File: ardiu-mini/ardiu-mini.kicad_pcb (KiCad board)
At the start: 2 copper layers, 69.9 x 25.4 mm, 39 parts, among them J1 Micro_SD_Card_Det, J2 ICSP, J3 Conn_01x06_Female, Q1 AO4838, Q2 AO4838, SW1 SW_Push, U1 ATmega328PB-A, U2 AP7375-33SA-7

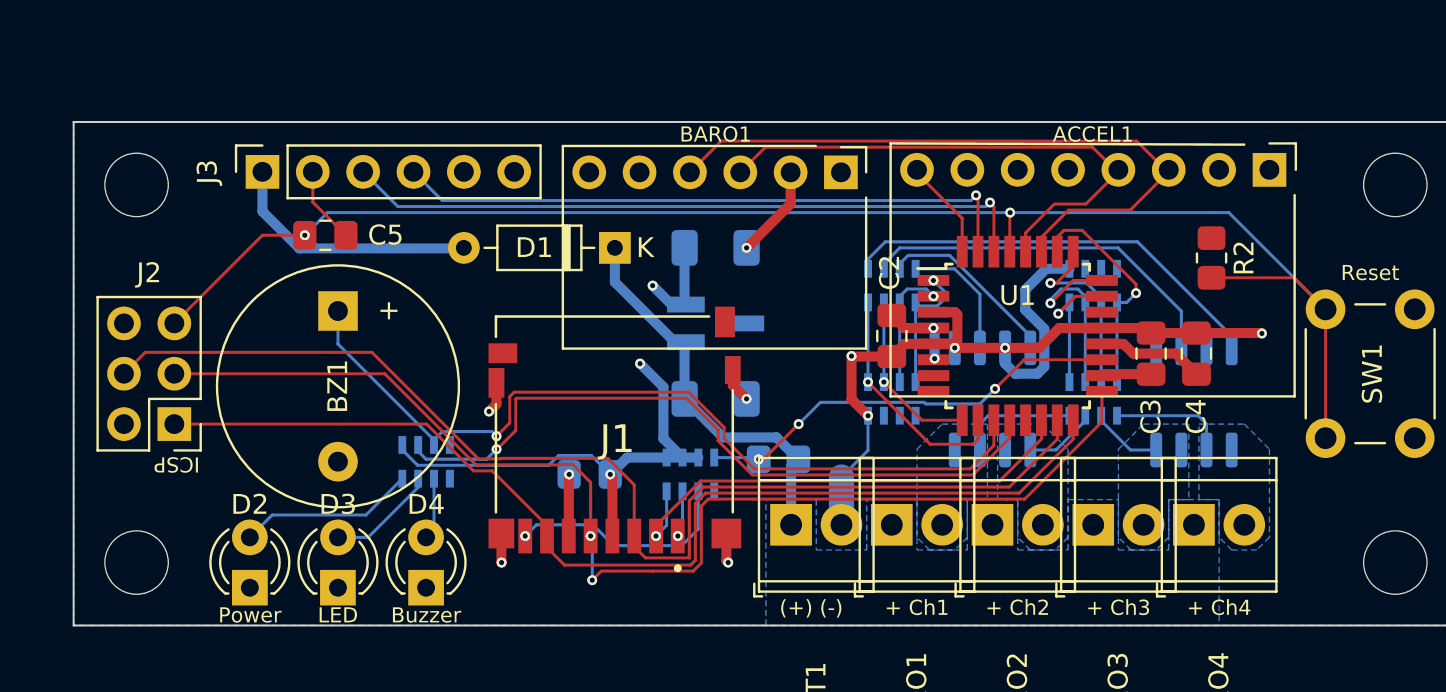
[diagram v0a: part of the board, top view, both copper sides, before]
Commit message: Fixed some errors, added actually 5V safe debug ports
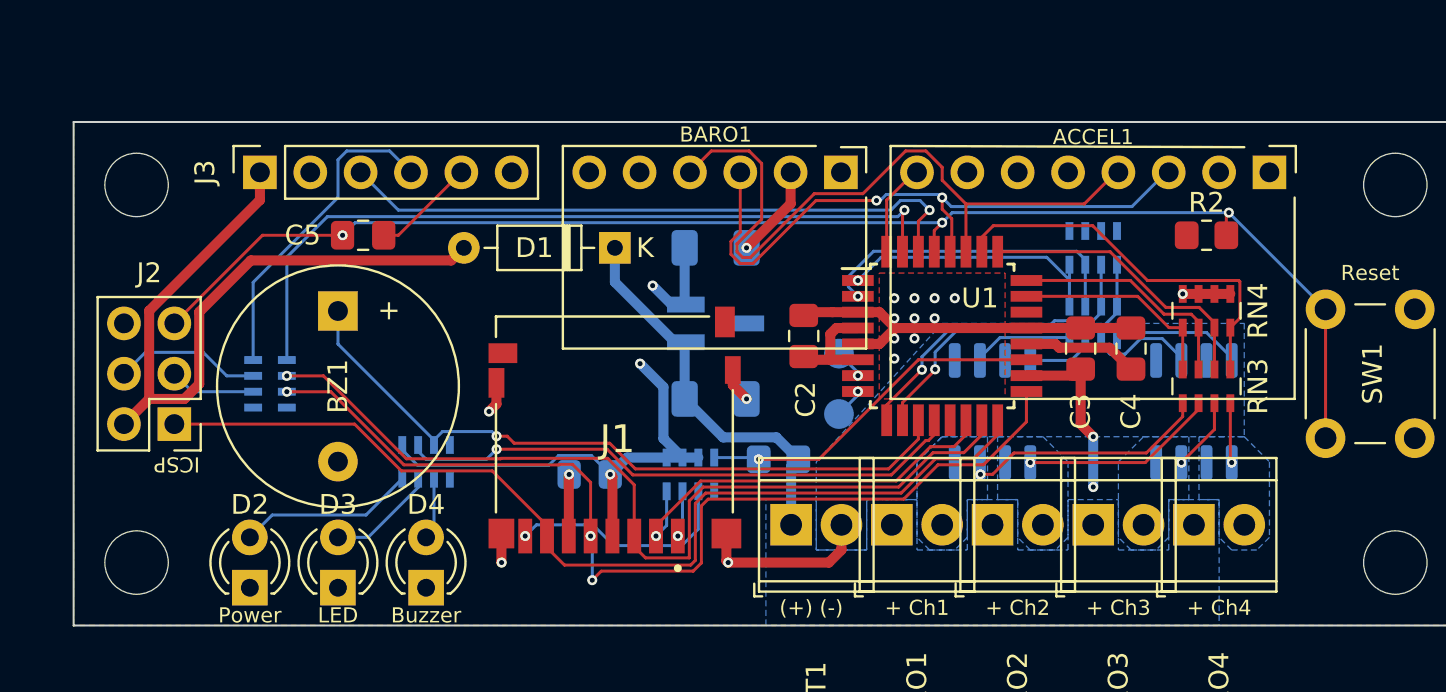
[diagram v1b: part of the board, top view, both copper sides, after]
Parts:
- added RN7: 2200, Resistor_SMD:R_Array_Concave_4x0603, B.Cu at (60.7, 114.8)
- added TPX1: x, TestPoint:TestPoint_Pad_D1.5mm, B.Cu at (89.4, 113.3)
- added TPX2: x, TestPoint:TestPoint_Pad_D1.5mm, B.Cu at (89.4, 116.3)
- R1: value R_US -> 100k
- RN3: value 10k -> 100k; moved to F.Cu
- RN4: moved to F.Cu
- moved RN1 12.7 mm to (102.2, 108.0), turned to -90 degrees
- moved RN2 10.3 mm to (102.2, 111.8), turned to -90 degrees
- moved RN4 5.85 mm to (108.0, 111.1)
- moved RN3 5.75 mm to (108.0, 114.9)
- moved C2 4.45 mm to (87.6, 112.4), turned to 90 degrees
- moved U1 3.81 mm to (94.6, 112.4)
- moved C3 3.57 mm to (101.6, 113.0)
- moved C4 3.31 mm to (104.1, 113.0)
- moved C5 1.91 mm to (65.4, 107.3), turned to 180 degrees
- moved R2 1.17 mm to (108.0, 107.3), turned to 0 degrees
- moved Q1 0.64 mm to (97.2, 116.2)
- moved Q2 0.64 mm to (107.3, 116.2)
- moved J3 0.13 mm to (60.2, 104.1)
- moved ACCEL1 0.13 mm to (111.1, 104.1)
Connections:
- ACCEL1 pad 3: /SDA -> /SCL
- ACCEL1 pad 4: /SCL -> /SDA
- C5 pad 1: /RST -> /DTR
- C5 pad 2: /DTR -> /RST
- J2 pad 2: +3V3 -> +5V
- J2 pad 3: /SCK -> /5SCK
- J2 pad 4: /MOSI -> /5MOSI
- J3 pad 2: /DTR -> GND
- J3 pad 4: /RX -> /5RX
- J3 pad 5: GND -> /DTR
- RN3 pad 1: /SENS1 -> /SENS4
- RN3 pad 2: /SENS2 -> /SENS3
- RN3 pad 3: /SENS3 -> /SENS2
- RN3 pad 4: /SENS4 -> /SENS1
- RN3 pad 5: /PYRO4 -> /PYRO1
- RN3 pad 6: /PYRO3 -> /PYRO2
- RN3 pad 7: /PYRO2 -> /PYRO3
- RN3 pad 8: /PYRO1 -> /PYRO4
- RN4 pad 5: /SENS4 -> /SENS1
- RN4 pad 6: /SENS3 -> /SENS2
- RN4 pad 7: /SENS2 -> /SENS3
- RN4 pad 8: /SENS1 -> /SENS4
- U1 pad 7: unconnected-(U1-Pad7) -> /XTAL1
- U1 pad 8: unconnected-(U1-Pad8) -> /XTAL2
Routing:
- net +5V: track 12.9 -> 36.7 mm
- net /5RX: track 0.00 -> 16.2 mm
- net GND: track 58.2 -> 42.9 mm, vias 11 -> 17
- net Net-(Q2-Pad4): track 21.8 -> 6.61 mm
- net Net-(Q2-Pad2): track 18.8 -> 5.34 mm
- net /MOSI: track 58.8 -> 45.7 mm, vias 0 -> 1
- net /CH2: track 6.33 -> 16.2 mm
- net /SCK: track 60.5 -> 50.6 mm, vias 2 -> 3
- net /SENS4: track 11.6 -> 19.8 mm, vias 1 -> 0
- net +3V3: track 36.7 -> 44.9 mm
- net /CH3: track 8.76 -> 16.3 mm
- net /RX: track 32.0 -> 39.5 mm
- net /5MOSI: track 0.00 -> 7.45 mm
- net /LED: track 36.4 -> 29.1 mm
- net /BUZ: track 42.7 -> 35.7 mm
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- added copper zone on F.Cu, net GND
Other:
- board text added: "ArdIU Mini 1.2 Designed by Ben Graham"
- board text removed: "ArdIU Mini 1.1 Designed by Ben Graham"
